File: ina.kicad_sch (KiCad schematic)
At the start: 23 parts

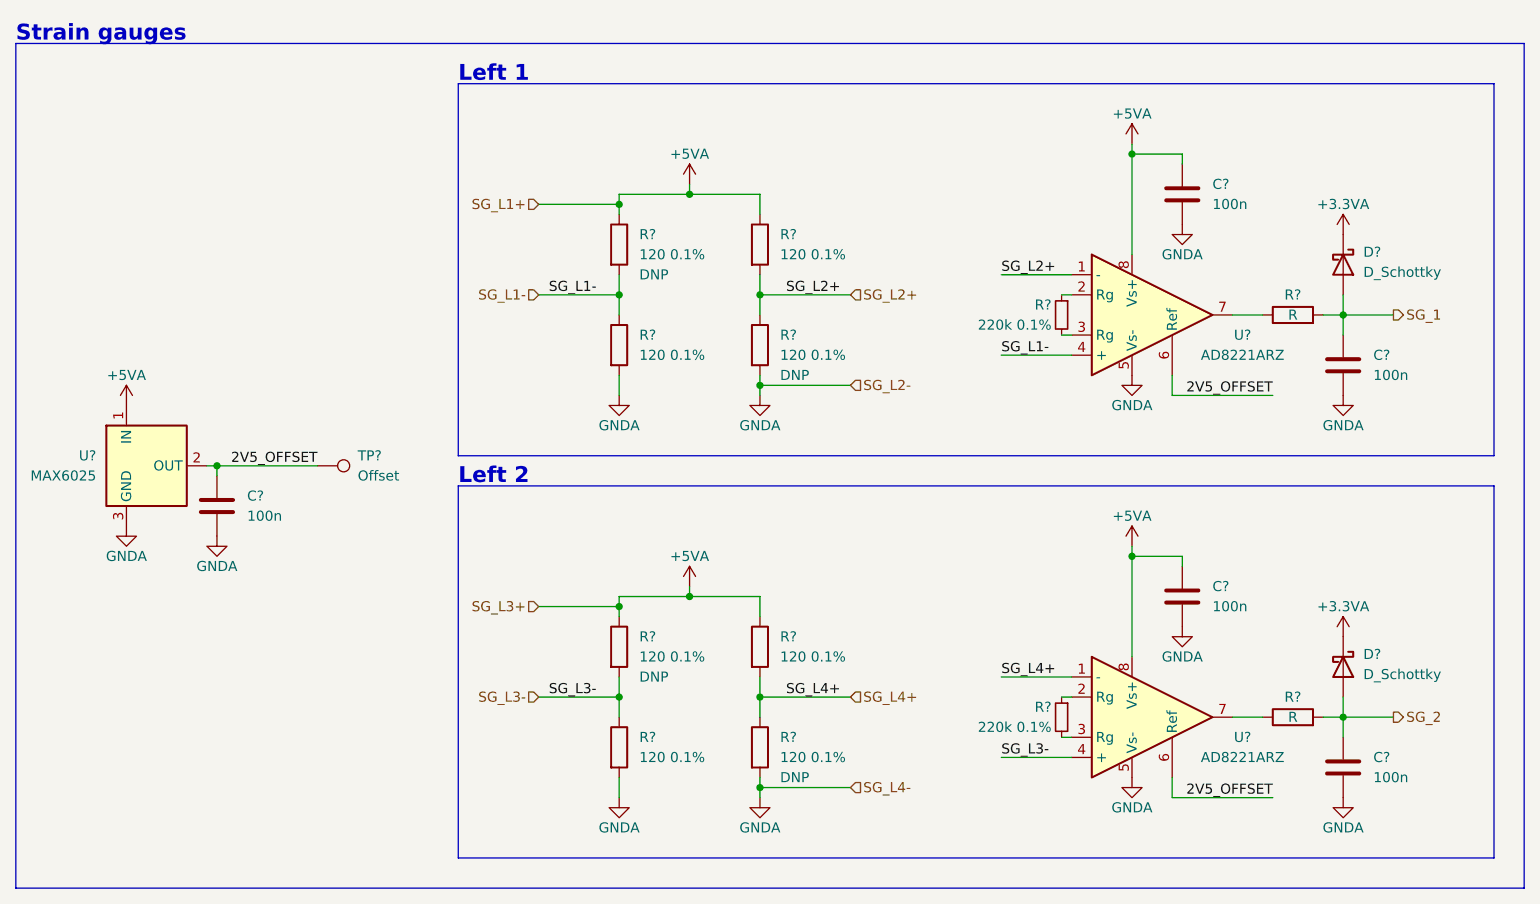
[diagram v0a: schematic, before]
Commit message: sch: input stage sheets
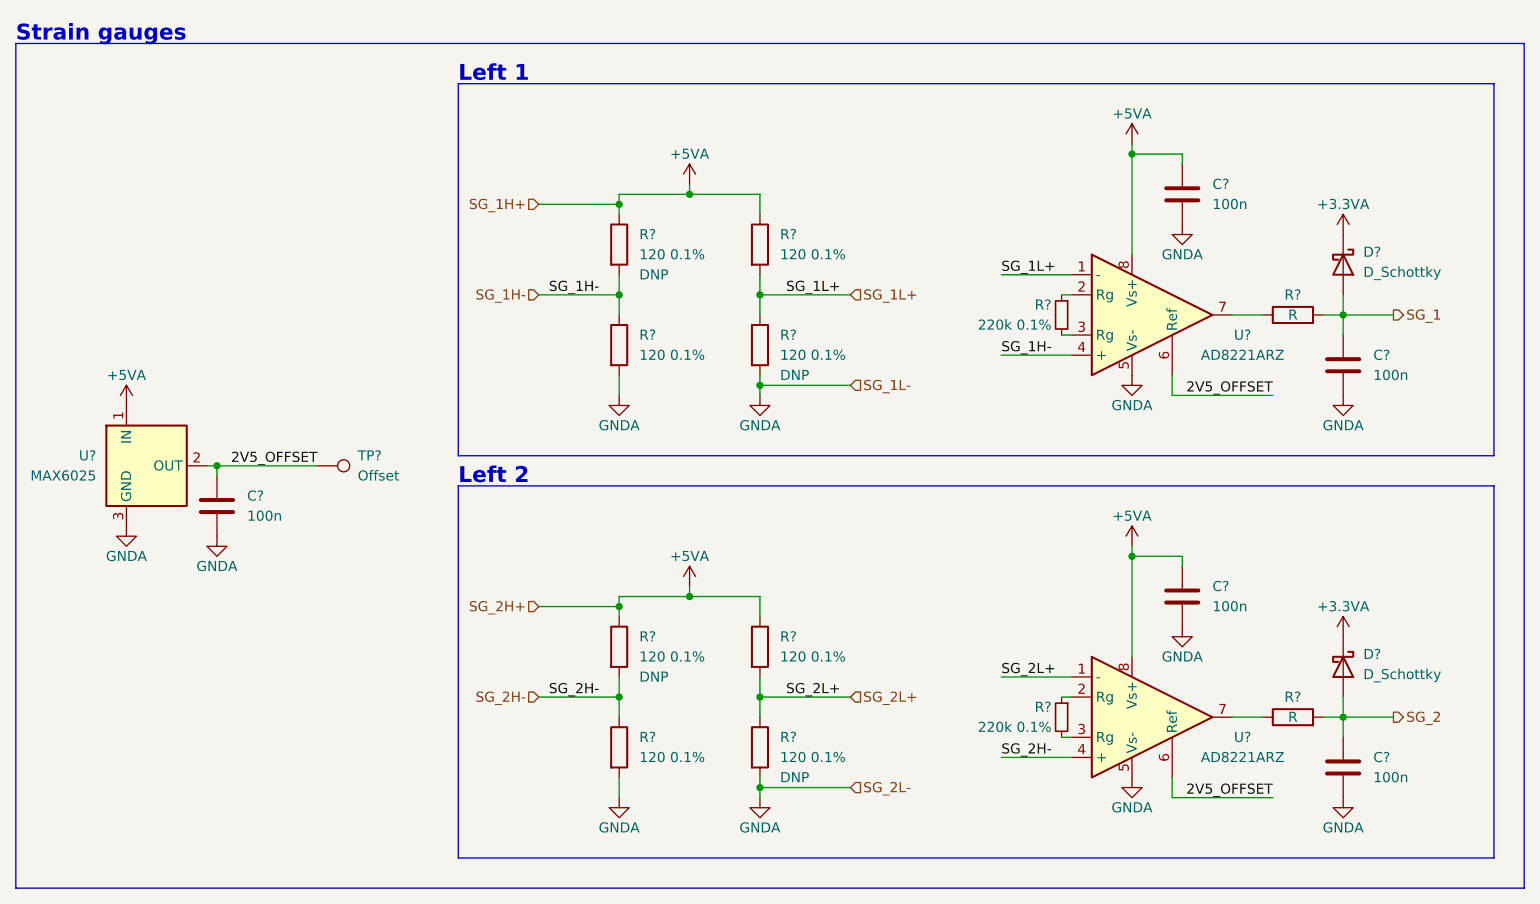
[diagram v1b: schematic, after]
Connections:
- net SG_L1- renamed SG_1H-
- net SG_L2+ renamed SG_1L+
- net SG_L3- renamed SG_2H-
- net SG_L4+ renamed SG_2L+
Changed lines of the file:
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@@
     (effects (font (size 2 2) (thickness 0.4) bold) (justify left bottom))
   )
-  (label "SG_L4+" (at 135.89 115.57 180)
+  (label "SG_2L+" (at 135.89 115.57 180)
     (effects (font (size 1.27 1.27)) (justify right bottom))
   )
-  (label "SG_L1-" (at 156.21 72.39 0)
+  (label "SG_1H-" (at 156.21 72.39 0)
     (effects (font (size 1.27 1.27)) (justify left bottom))
   )
-  (label "SG_L3-" (at 99.06 115.57 0)
+  (label "SG_2H-" (at 99.06 115.57 0)
     (effects (font (size 1.27 1.27)) (justify left bottom))
   )
-  (label "SG_L4+" (at 156.21 113.03 0)
+  (label "SG_2L+" (at 156.21 113.03 0)
     (effects (font (size 1.27 1.27)) (justify left bottom))
   )
-  (label "SG_L3-" (at 156.21 123.19 0)
+  (label "SG_2H-" (at 156.21 123.19 0)
     (effects (font (size 1.27 1.27)) (justify left bottom))
   )
-  (label "SG_L1-" (at 99.06 64.77 0)
+  (label "SG_1H-" (at 99.06 64.77 0)
     (effects (font (size 1.27 1.27)) (justify left bottom))
   )
@@
     (effects (font (size 1.27 1.27)) (justify right bottom))
   )
-  (label "SG_L2+" (at 156.21 62.23 0)
+  (label "SG_1L+" (at 156.21 62.23 0)
     (effects (font (size 1.27 1.27)) (justify left bottom))
   )
@@
     (effects (font (size 1.27 1.27)) (justify right bottom))
   )
-  (label "SG_L2+" (at 135.89 64.77 180)
+  (label "SG_1L+" (at 135.89 64.77 180)
     (effects (font (size 1.27 1.27)) (justify right bottom))
   )
@@
     (effects (font (size 1.27 1.27)) (justify right bottom))
   )
-  (hierarchical_label "SG_L2-" (shape input) (at 137.16 76.2 0)
+  (hierarchical_label "SG_1L-" (shape input) (at 137.16 76.2 0)
     (effects (font (size 1.27 1.27)) (justify left))
   )
@@
     (effects (font (size 1.27 1.27)) (justify left))
   )
-  (hierarchical_label "SG_L4+" (shape input) (at 137.16 115.57 0)
+  (hierarchical_label "SG_2L+" (shape input) (at 137.16 115.57 0)
     (effects (font (size 1.27 1.27)) (justify left))
   )
-  (hierarchical_label "SG_L3+" (shape input) (at 97.79 104.14 180)
+  (hierarchical_label "SG_2H+" (shape input) (at 97.79 104.14 180)
     (effects (font (size 1.27 1.27)) (justify right))
   )
-  (hierarchical_label "SG_L1+" (shape input) (at 97.79 53.34 180)
+  (hierarchical_label "SG_1H+" (shape input) (at 97.79 53.34 180)
     (effects (font (size 1.27 1.27)) (justify right))
   )
-  (hierarchical_label "SG_L2+" (shape input) (at 137.16 64.77 0)
+  (hierarchical_label "SG_1L+" (shape input) (at 137.16 64.77 0)
     (effects (font (size 1.27 1.27)) (justify left))
   )
-  (hierarchical_label "SG_L3-" (shape input) (at 97.79 115.57 180)
+  (hierarchical_label "SG_2H-" (shape input) (at 97.79 115.57 180)
     (effects (font (size 1.27 1.27)) (justify right))
   )
-  (hierarchical_label "SG_L1-" (shape input) (at 97.79 64.77 180)
+  (hierarchical_label "SG_1H-" (shape input) (at 97.79 64.77 180)
     (effects (font (size 1.27 1.27)) (justify right))
   )
-  (hierarchical_label "SG_L4-" (shape input) (at 137.16 127 0)
+  (hierarchical_label "SG_2L-" (shape input) (at 137.16 127 0)
     (effects (font (size 1.27 1.27)) (justify left))
   )
